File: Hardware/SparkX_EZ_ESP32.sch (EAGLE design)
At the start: 57 parts, among them Q1 MBT3904DW1T1, U1 3.3V, U2 ESP32, U3 W25QXX128MBIT-6X5, U4 CP210X, X1 32.768kHz, X2 40MHz

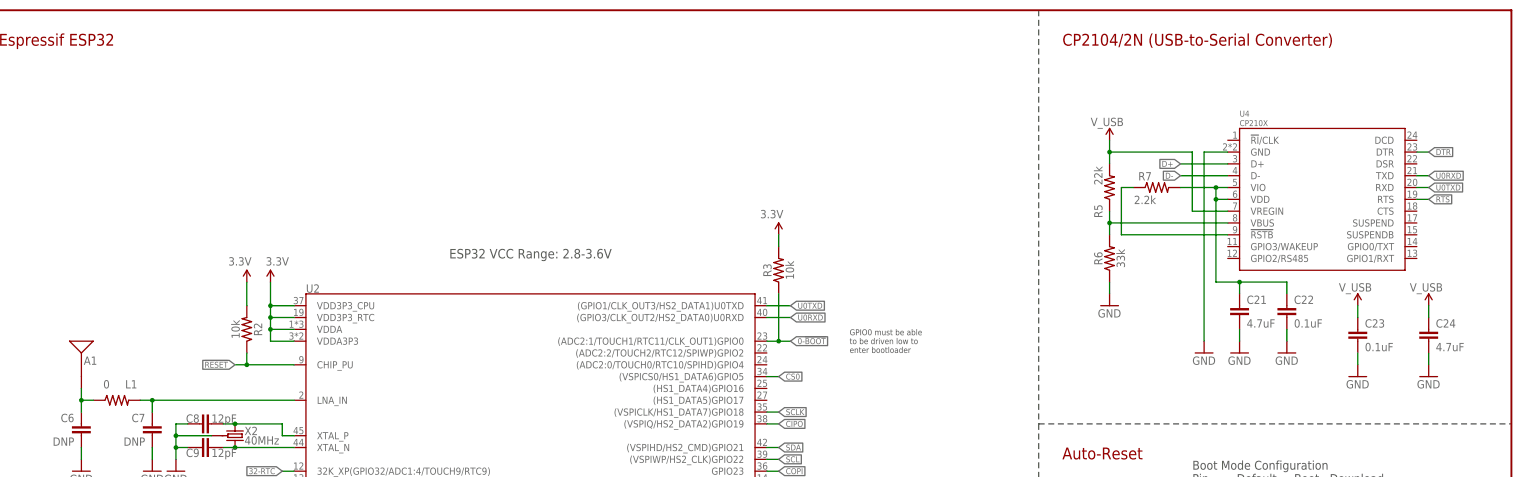
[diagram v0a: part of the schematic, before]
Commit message: Add CP2102 package outline
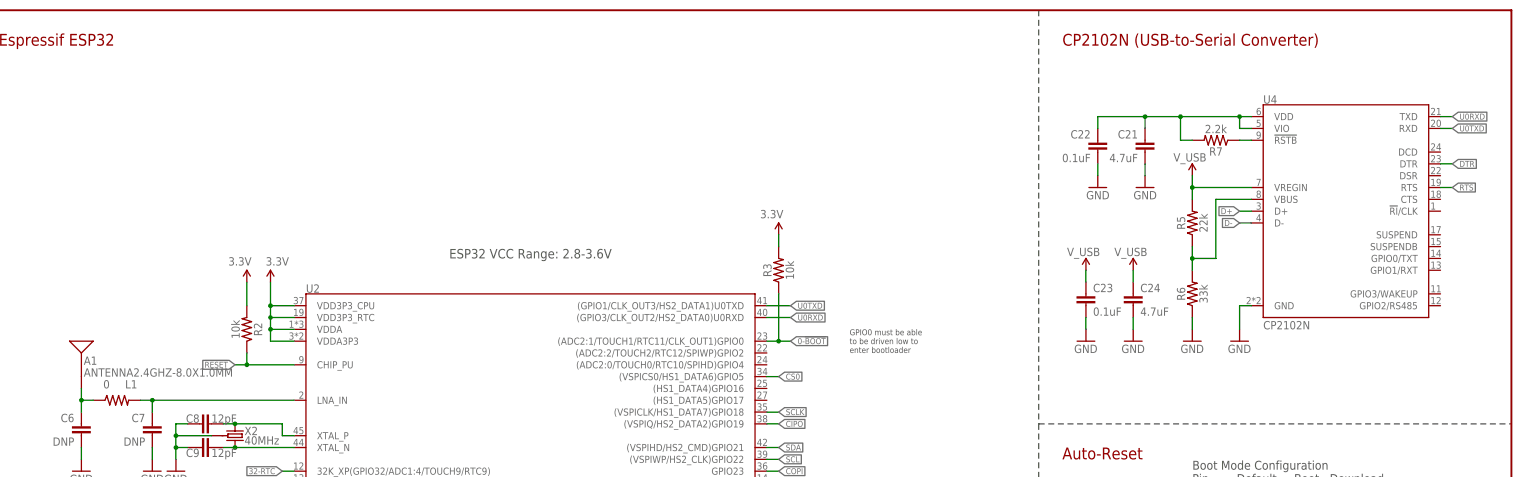
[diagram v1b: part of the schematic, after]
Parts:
- U3: device SparkFun-MicroMod:W25QXX128MBIT-6X5 -> SparkFun-IC-Memory:W25QXX128MBIT-6X5
- U4: value CP210X -> CP2102N
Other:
- note added: "CP2102N (USB-to-Serial Converter)"
- note removed: "CP2104/2N (USB-to-Serial Converter)"
- moved on the sheet: C21, C22, C23, C24, R5, R6, R7, U4

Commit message: Routed
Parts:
- added !BOOT!, !RESET!, FLASH_VDD, RXT, TXT, USB_3V3: TEST-POINT3X4, SparkFun-Connectors:TEST-POINT3X4
- U3: value W25QXX128MBIT-6X5 -> W25QXX128MBIT-6X5-SKINNY_CENTER; device SparkFun-IC-Memory:W25QXX128MBIT-6X5 -> SparkFun-IC-Memory:W25QXX128MBIT-6X5-SKINNY_CENTER
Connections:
- net 39-BATT/3 renamed N$3
- new net RXT: RXT.1, U4.GPIO1/RXT
- new net TXT: TXT.1, U4.GPIO0/TXT
- net !RESET: now also !RESET!.1
- net 0-!BOOT!: now also !BOOT!.1
- net FLASH_VDD: now also FLASH_VDD.1
- net USB_3V3: now also USB_3V3.1
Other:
- note added: "RF Track Impedance: Coplanar Waveguide with Ground Calculations https://chemandy.com/calculators/coplanar-waveguide-with-ground-calculator.htm ---------------- JLCPCB JLC7628 4-Layer 1.6mm Impedance Control Stackup (Er = 4.6) ---------------- Ground is on layer 2. Prepreg thickness: 0.2mm 12 mil track with 4 mil gap = 49.5 Ohms"
- note removed: "RF Track Impedance: Coplanar Waveguide with Ground Calculations https://chemandy.com/calculators/coplanar-waveguide-with-ground-calculator.htm ---------------- JLCPCB JLC7628 4-Layer 0.8mm Impedance Control Stackup (Er = 4.6) ---------------- Ground is on layer 2. Prepreg thickness: 0.2mm 12 mil track with 4 mil gap = 49.5 Ohms"
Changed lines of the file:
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@@
 <setting verticaltext="up"/>
 </settings>
-<grid distance="0.1" unitdist="inch" unit="inch" style="lines" multiple="1" display="no" altdistance="0.05" altunitdist="inch" altunit="inch"/>
+<grid distance="0.05" unitdist="inch" unit="inch" style="lines" multiple="1" display="yes" altdistance="0.005" altunitdist="inch" altunit="inch"/>
 <layers>
 <layer number="1" name="Top" color="4" fill="1" visible="no" active="no"/>
@@
 <part name="SUPPLY63" library="SparkFun-PowerSymbols" deviceset="V_USB" device=""/>
 <part name="R7" library="SparkFun-Resistors" deviceset="2.2KOHM" device="-0402T-1/16W-1%" value="2.2k"/>
-<part name="U3" library="SparkFun-IC-Memory" deviceset="W25QXX" device="128MBIT-6X5"/>
+<part name="U3" library="SparkFun-IC-Memory" deviceset="W25QXX" device="128MBIT-6X5-SKINNY_CENTER" value="W25QXX128MBIT-6X5-SKINNY_CENTER"/>
 <part name="L1" library="SparkFun-Resistors" deviceset="0OHM" device="-0402T-1/10W" value="0"/>
 <part name="GND138" library="SparkFun-PowerSymbols" deviceset="GND" device=""/>
@@
 <part name="R1" library="SparkFun-Resistors" deviceset="100KOHM" device="-0402T-1/16W-1%" value="100k"/>
 <part name="U4" library="SparkFun-IC-Comms" deviceset="CP2102N" device=""/>
+<part name="TXT" library="SparkFun-Connectors" deviceset="TEST-POINT" device="3X4" value="TEST-POINT3X4"/>
+<part name="RXT" library="SparkFun-Connectors" deviceset="TEST-POINT" device="3X4" value="TEST-POINT3X4"/>
+<part name="!BOOT!" library="SparkFun-Connectors" deviceset="TEST-POINT" device="3X4" value="TEST-POINT3X4"/>
+<part name="!RESET!" library="SparkFun-Connectors" deviceset="TEST-POINT" device="3X4" value="TEST-POINT3X4"/>
+<part name="USB_3V3" library="SparkFun-Connectors" deviceset="TEST-POINT" device="3X4" value="TEST-POINT3X4"/>
+<part name="FLASH_VDD" library="SparkFun-Connectors" deviceset="TEST-POINT" device="3X4" value="TEST-POINT3X4"/>
 </parts>
 <sheets>
@@
 https://chemandy.com/calculators/coplanar-waveguide-with-ground-calculator.htm
 ----------------
-JLCPCB JLC7628 4-Layer 0.8mm Impedance Control Stackup (Er = 4.6)
+JLCPCB JLC7628 4-Layer 1.6mm Impedance Control Stackup (Er = 4.6)
 ----------------
 Ground is on layer 2.
@@
 <instance part="A1" gate="G$1" x="124.46" y="203.2" smashed="yes">
 <attribute name="NAME" x="124.968" y="203.2" size="1.778" layer="95" font="vector"/>
-<attribute name="VALUE" x="124.968" y="200.66" size="1.778" layer="96" font="vector"/>
+<attribute name="VALUE" x="105.918" y="210.82" size="1.778" layer="96" font="vector"/>
 </instance>
 <instance part="C6" gate="G$1" x="124.46" y="187.96" smashed="yes" rot="MR0">
@@
 <attribute name="NAME" x="378.46" y="259.334" size="1.778" layer="95"/>
 <attribute name="VALUE" x="378.46" y="210.82" size="1.778" layer="96"/>
+</instance>
+<instance part="TXT" gate="G$1" x="419.1" y="226.06" smashed="yes">
+<attribute name="NAME" x="424.18" y="224.79" size="1.778" layer="95" font="vector"/>
+</instance>
+<instance part="RXT" gate="G$1" x="419.1" y="223.52" smashed="yes">
+<attribute name="NAME" x="424.18" y="222.25" size="1.778" layer="95" font="vector"/>
+</instance>
+<instance part="!BOOT!" gate="G$1" x="375.92" y="114.3" smashed="yes">
+<attribute name="NAME" x="381" y="113.03" size="1.778" layer="95" font="vector"/>
+</instance>
+<instance part="!RESET!" gate="G$1" x="375.92" y="147.32" smashed="yes">
+<attribute name="NAME" x="381" y="146.05" size="1.778" layer="95" font="vector"/>
+</instance>
+<instance part="USB_3V3" gate="G$1" x="360.68" y="260.35" smashed="yes" rot="R90">
+<attribute name="NAME" x="363.22" y="261.62" size="1.778" layer="95" font="vector"/>
+</instance>
+<instance part="FLASH_VDD" gate="G$1" x="35.56" y="114.3" smashed="yes" rot="R90">
+<attribute name="NAME" x="30.48" y="119.38" size="1.778" layer="95" font="vector"/>
 </instance>
 </instances>
@@
 <label x="370.84" y="147.32" size="1.27" layer="95" font="vector" rot="R180" xref="yes"/>
 <pinref part="Q1" gate="Q1" pin="C"/>
+<pinref part="!RESET!" gate="G$1" pin="1"/>
+<wire x1="375.92" y1="147.32" x2="373.38" y2="147.32" width="0.1524" layer="91"/>
+<junction x="373.38" y="147.32"/>
 </segment>
 </net>
@@
 <junction x="55.88" y="170.18"/>
 <label x="58.42" y="170.18" size="1.27" layer="95" font="vector" xref="yes"/>
-</segment>
-</net>
-<net name="39-BATT/3" class="0">
-<segment>
-<pinref part="U2" gate="G$1" pin="SENSOR_VN(GPI39/ADC1:3/RTC3)"/>
-<pinref part="C11" gate="G$1" pin="2"/>
-<wire x1="149.86" y1="152.4" x2="149.86" y2="149.86" width="0.1524" layer="91"/>
-<wire x1="149.86" y1="149.86" x2="152.4" y2="149.86" width="0.1524" layer="91"/>
-<wire x1="152.4" y1="149.86" x2="152.4" y2="152.4" width="0.1524" layer="91"/>
-<wire x1="152.4" y1="152.4" x2="170.18" y2="152.4" width="0.1524" layer="91"/>
 </segment>
 </net>
@@
 <pinref part="Q1" gate="Q2" pin="C"/>
 <wire x1="373.38" y1="114.3" x2="373.38" y2="116.84" width="0.1524" layer="91"/>
+<pinref part="!BOOT!" gate="G$1" pin="1"/>
+<wire x1="375.92" y1="114.3" x2="373.38" y2="114.3" width="0.1524" layer="91"/>
+<junction x="373.38" y="114.3"/>
 </segment>
 </net>
@@
 <junction x="35.56" y="111.76"/>
 <label x="33.02" y="111.76" size="1.27" layer="95" rot="R180" xref="yes"/>
+<pinref part="FLASH_VDD" gate="G$1" pin="1"/>
+<wire x1="35.56" y1="114.3" x2="35.56" y2="111.76" width="0.1524" layer="91"/>
 </segment>
 <segment>
@@
 <wire x1="373.38" y1="254" x2="373.38" y2="256.54" width="0.1524" layer="91"/>
 <junction x="373.38" y="256.54"/>
-</segment>
-</net>
+<pinref part="USB_3V3" gate="G$1" pin="1"/>
+<wire x1="360.68" y1="260.35" x2="360.68" y2="256.54" width="0.1524" layer="91"/>
+</segment>
+</net>
+<net name="N$3" class="0">
+<segment>
+<pinref part="U2" gate="G$1" pin="SENSOR_VN(GPI39/ADC1:3/RTC3)"/>
+<wire x1="170.18" y1="152.4" x2="152.4" y2="152.4" width="0.1524" layer="91"/>
+<wire x1="152.4" y1="152.4" x2="152.4" y2="149.86" width="0.1524" layer="91"/>
+<wire x1="152.4" y1="149.86" x2="149.86" y2="149.86" width="0.1524" layer="91"/>
+<pinref part="C11" gate="G$1" pin="2"/>
+<wire x1="149.86" y1="149.86" x2="149.86" y2="152.4" width="0.1524" layer="91"/>
+</segment>
+</net>
+<net name="TXT" class="0">
+<segment>
+<pinref part="U4" gate="G$1" pin="GPIO0/TXT"/>
+<pinref part="TXT" gate="G$1" pin="1"/>
+<wire x1="416.56" y1="226.06" x2="419.1" y2="226.06" width="0.1524" layer="91"/>
+</segment>
+</net>
+<net name="RXT" class="0">
+<segment>
+<pinref part="U4" gate="G$1" pin="GPIO1/RXT"/>
+<pinref part="RXT" gate="G$1" pin="1"/>
+<wire x1="416.56" y1="223.52" x2="419.1" y2="223.52" width="0.1524" layer="91"/>
+</segment>
+</net>

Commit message: Add neopixel. Add mirror-symmetric production panel
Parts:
- added C25: 0.1uF, SparkFun-Capacitors:0.1UF-0402T-16V-10%
- added D1: WS2812_2020, SparkFun-LED:WS2812_2020
- added LED_DO: TEST-POINT3X4, SparkFun-Connectors:TEST-POINT3X4
- added LOGO4: SPECIAL_INSTRUCTIONS-PRODUCTION, SparkFun-Aesthetics:SPECIAL_INSTRUCTIONS-PRODUCTION
- U1: value 3.3V -> MIC5219 3.3V; device SparkFun-IC-Power:V_REG_AP2112K-3.3V -> SparkFun-IC-Power:V_REG_MIC52193.3V
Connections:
- new net LED: D1.DI, U2.(DAC1/ADC2:8/RTC6)GPIO25
- new net N$4: D1.DO, LED_DO.1
- net 3.3V: now also C25.1, D1.VCC
- net GND: now also C25.2, D1.GND
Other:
- note added: "MIC5219-3.3V ------------- Iout (max): 500mA Vin (max): 12V Vdrop (typ @ 500mA): 350mV Vdrop (max @ 500mA): 500mV Iq (typ): 80uA Output discharge: None"
- note added: "RF Track Impedance: Coplanar Waveguide with Ground Calculations https://chemandy.com/calculators/coplanar-waveguide-with-ground-calculator.htm ---------------- JLCPCB JLC7628 4-Layer 1.2mm Impedance Control Stackup (Er = 4.6) ---------------- Ground is on layer 2. Prepreg thickness: 0.2mm 12 mil track with 4 mil gap = 49.5 Ohms"
- note added: "RGB LED"
- note removed: "AP2112K-3.3V ------------- Iout (max): 600mA Vin (max): 6.5V Vdrop (max): 250mV Iq: 55uA"
- note removed: "RF Track Impedance: Coplanar Waveguide with Ground Calculations https://chemandy.com/calculators/coplanar-waveguide-with-ground-calculator.htm ---------------- JLCPCB JLC7628 4-Layer 1.6mm Impedance Control Stackup (Er = 4.6) ---------------- Ground is on layer 2. Prepreg thickness: 0.2mm 12 mil track with 4 mil gap = 49.5 Ohms"
- moved on the sheet: C3, C4, C5, FLASH_VDD, U3, X1

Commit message: Post-review updates
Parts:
- C1: value 0.1uF -> 2.2uF; device SparkFun-Capacitors:0.1UF-0402T-10V-10%-X7R -> SparkFun-Capacitors:2.2UF-0402_TIGHT-10V-10%-X5R
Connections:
- net CS1: now also U2.(GPIO14/ADC2:6/TOUCH6/RTC16/SPICLK)MTMS; no longer U2.(DAC2/ADC2:9/RTC7)GPIO26
- net CS2: now also U2.(GPIO13/ADC2:4/TOUCH4/RTC14/SPID/U0CTS)MTCK; no longer U2.(ADC2:7/TOUCH7/RTC17)GPIO27
- net GPIO0: now also U2.(ADC2:7/TOUCH7/RTC17)GPIO27; no longer U2.VDET_1(GPI34/ADC1:6)
- net GPIO1: now also U2.(DAC2/ADC2:9/RTC7)GPIO26; no longer U2.VDET_2(GPI35/ADC1:7)

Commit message: Update 16-way FPC Connector
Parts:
- IN, OUT: value FPC_16_0.5MM_BACKFLIP -> (none); device New_Parts_Connectors:FPC_16_0.5MM_BACKFLIP -> SparkFun-Connectors:CONN_16FPC_16_0.5MM
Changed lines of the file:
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@@
 <part name="FD3" library="SparkFun-Aesthetics" deviceset="FIDUCIAL" device="UFIDUCIAL" value="FIDUCIALUFIDUCIAL"/>
 <part name="FD4" library="SparkFun-Aesthetics" deviceset="FIDUCIAL" device="UFIDUCIAL" value="FIDUCIALUFIDUCIAL"/>
-<part name="IN" library="New_Parts_Connectors" deviceset="FPC_16_0.5MM" device="_BACKFLIP"/>
-<part name="OUT" library="New_Parts_Connectors" deviceset="FPC_16_0.5MM" device="_BACKFLIP"/>
+<part name="IN" library="SparkFun-Connectors" deviceset="CONN_16" device="FPC_16_0.5MM"/>
+<part name="OUT" library="SparkFun-Connectors" deviceset="CONN_16" device="FPC_16_0.5MM"/>
 <part name="SUPPLY21" library="SparkFun-PowerSymbols" deviceset="3.3V" device=""/>
 <part name="SUPPLY22" library="SparkFun-PowerSymbols" deviceset="3.3V" device=""/>
@@
 <instance part="LOGO3" gate="G$1" x="307.34" y="25.4" smashed="yes"/>
 <instance part="U$4" gate="G$1" x="307.34" y="7.62" smashed="yes"/>
-<instance part="IN" gate="G$1" x="20.32" y="35.56" smashed="yes">
-<attribute name="NAME" x="17.78" y="56.134" size="1.778" layer="95"/>
-<attribute name="VALUE" x="17.78" y="10.16" size="1.778" layer="96"/>
-</instance>
-<instance part="OUT" gate="G$1" x="78.74" y="35.56" smashed="yes" rot="MR0">
-<attribute name="NAME" x="81.28" y="56.134" size="1.778" layer="95" rot="MR0"/>
-<attribute name="VALUE" x="81.28" y="10.16" size="1.778" layer="96" rot="MR0"/>
+<instance part="IN" gate="G$1" x="17.78" y="33.02" smashed="yes" rot="MR180">
+<attribute name="NAME" x="17.78" y="12.446" size="1.778" layer="95" rot="MR180"/>
+<attribute name="VALUE" x="15.24" y="58.42" size="1.778" layer="96" rot="MR180"/>
+</instance>
+<instance part="OUT" gate="G$1" x="81.28" y="33.02" smashed="yes" rot="R180">
+<attribute name="NAME" x="81.28" y="12.446" size="1.778" layer="95" rot="R180"/>
+<attribute name="VALUE" x="83.82" y="58.42" size="1.778" layer="96" rot="R180"/>
 </instance>
 <instance part="SUPPLY21" gate="G$1" x="30.48" y="55.88" smashed="yes">
@@
 <segment>
 <pinref part="SUPPLY21" gate="G$1" pin="3.3V"/>
-<wire x1="30.48" y1="55.88" x2="30.48" y2="50.8" width="0.1524" layer="91"/>
 <pinref part="IN" gate="G$1" pin="2"/>
-<wire x1="30.48" y1="50.8" x2="27.94" y2="50.8" width="0.1524" layer="91"/>
 <pinref part="IN" gate="G$1" pin="15"/>
 <wire x1="27.94" y1="17.78" x2="30.48" y2="17.78" width="0.1524" layer="91"/>
 <wire x1="30.48" y1="17.78" x2="30.48" y2="50.8" width="0.1524" layer="91"/>
+<wire x1="30.48" y1="50.8" x2="30.48" y2="55.88" width="0.1524" layer="91"/>
+<wire x1="27.94" y1="50.8" x2="30.48" y2="50.8" width="0.1524" layer="91"/>
 <junction x="30.48" y="50.8"/>
 </segment>
 <segment>
 <pinref part="SUPPLY22" gate="G$1" pin="3.3V"/>
-<wire x1="68.58" y1="55.88" x2="68.58" y2="50.8" width="0.1524" layer="91"/>
 <pinref part="OUT" gate="G$1" pin="2"/>
-<wire x1="68.58" y1="50.8" x2="71.12" y2="50.8" width="0.1524" layer="91"/>
 <pinref part="OUT" gate="G$1" pin="15"/>
 <wire x1="71.12" y1="17.78" x2="68.58" y2="17.78" width="0.1524" layer="91"/>
 <wire x1="68.58" y1="17.78" x2="68.58" y2="50.8" width="0.1524" layer="91"/>
+<wire x1="68.58" y1="50.8" x2="68.58" y2="55.88" width="0.1524" layer="91"/>
+<wire x1="71.12" y1="50.8" x2="68.58" y2="50.8" width="0.1524" layer="91"/>
 <junction x="68.58" y="50.8"/>
 </segment>
@@
 <pinref part="IN" gate="G$1" pin="16"/>
 <wire x1="27.94" y1="15.24" x2="30.48" y2="15.24" width="0.1524" layer="91"/>
-<wire x1="30.48" y1="12.7" x2="30.48" y2="15.24" width="0.1524" layer="91"/>
-</segment>
-<segment>
+<wire x1="30.48" y1="15.24" x2="30.48" y2="12.7" width="0.1524" layer="91"/>
+</segment>
+<segment>
